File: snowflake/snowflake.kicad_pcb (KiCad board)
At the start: 2 copper layers, 150.2 x 150.2 mm, 85 parts, among them J3 TC2030, SW1 SK-12E12-G040, U1 TZ-5050S2RGB-5V-I4-H1, U10 TZ-5050S2RGB-5V-I4-H1, U11 TZ-5050S2RGB-5V-I4-H1, U12 TZ-5050S2RGB-5V-I4-H1, U13 TZ-5050S2RGB-5V-I4-H1, U14 TZ-5050S2RGB-5V-I4-H1, U15 TZ-5050S2RGB-5V-I4-H1, U16 TZ-5050S2RGB-5V-I4-H1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

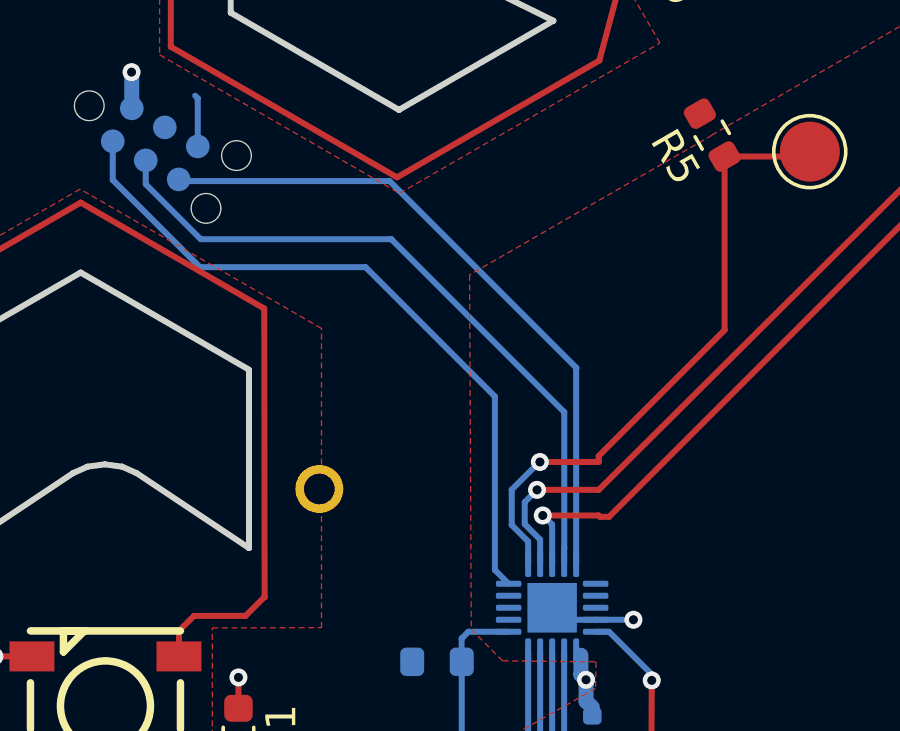
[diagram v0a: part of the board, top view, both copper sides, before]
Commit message: Add more vias to try and keep the ground planes even
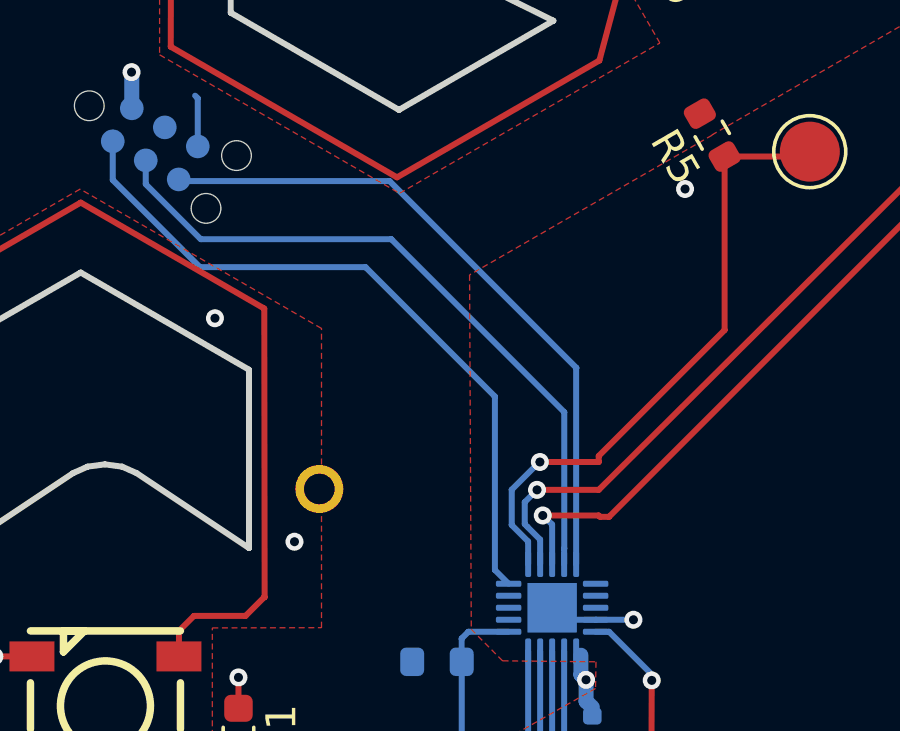
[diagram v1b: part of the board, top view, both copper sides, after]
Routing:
- net GND: vias 50 -> 53
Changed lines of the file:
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@@
+	)
+	(via
+		(at 135.090399 132.750272)
+		(size 0.6)
+		(drill 0.3)
+		(layers "F.Cu" "B.Cu")
+		(free yes)
+		(net 2)
 	)
 	(via
@@
 		(net 2)
 	)
+	(via
+		(at 122.071621 144.507554)
+		(size 0.6)
+		(drill 0.3)
+		(layers "F.Cu" "B.Cu")
+		(free yes)
+		(net 2)
+	)
+	(via
+		(at 119.420449 137.058398)
+		(size 0.6)
+		(drill 0.3)
+		(layers "F.Cu" "B.Cu")
+		(free yes)
+		(net 2)
+	)

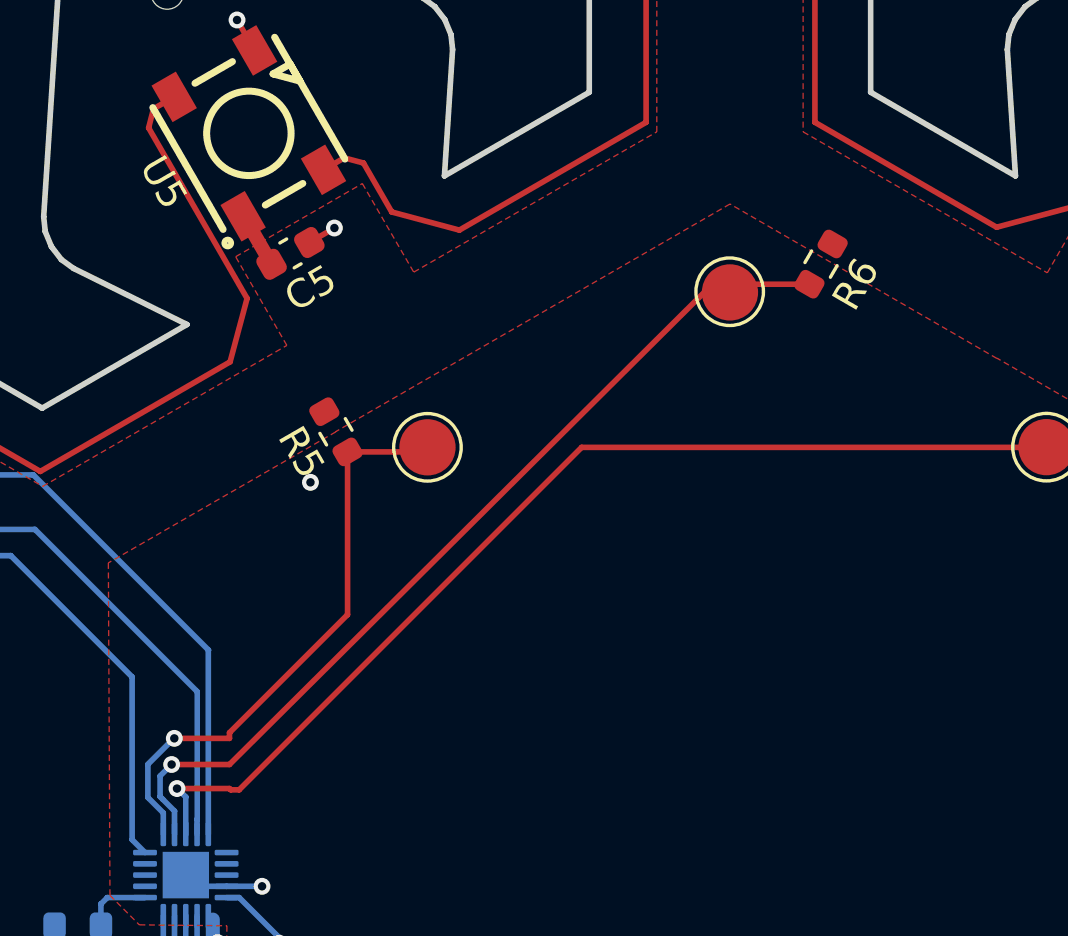
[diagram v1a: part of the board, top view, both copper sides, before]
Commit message: Add teardrops to vias and PTH pads, mask border
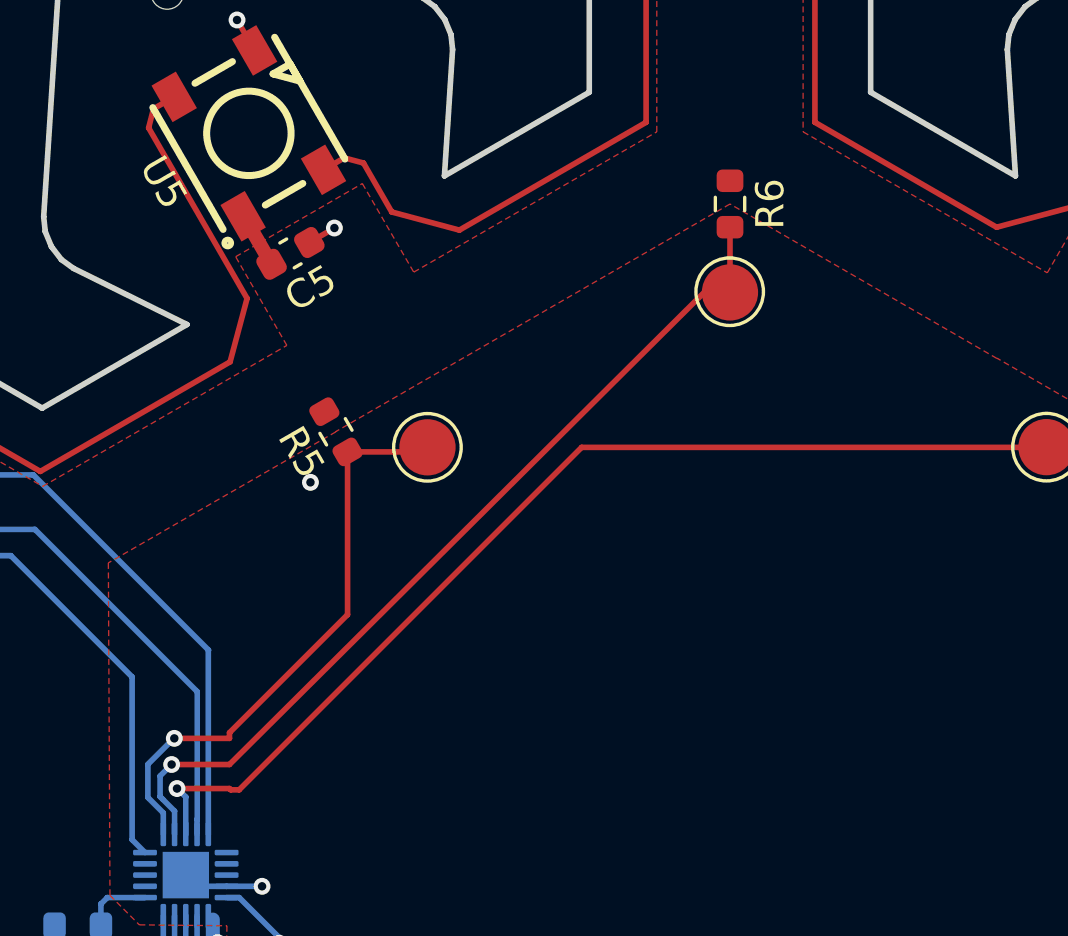
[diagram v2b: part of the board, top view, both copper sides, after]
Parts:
- moved R6 3.88 mm to (150.0, 122.9), turned to -90 degrees
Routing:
- net /TOUCH2: track 32.6 -> 32.0 mm

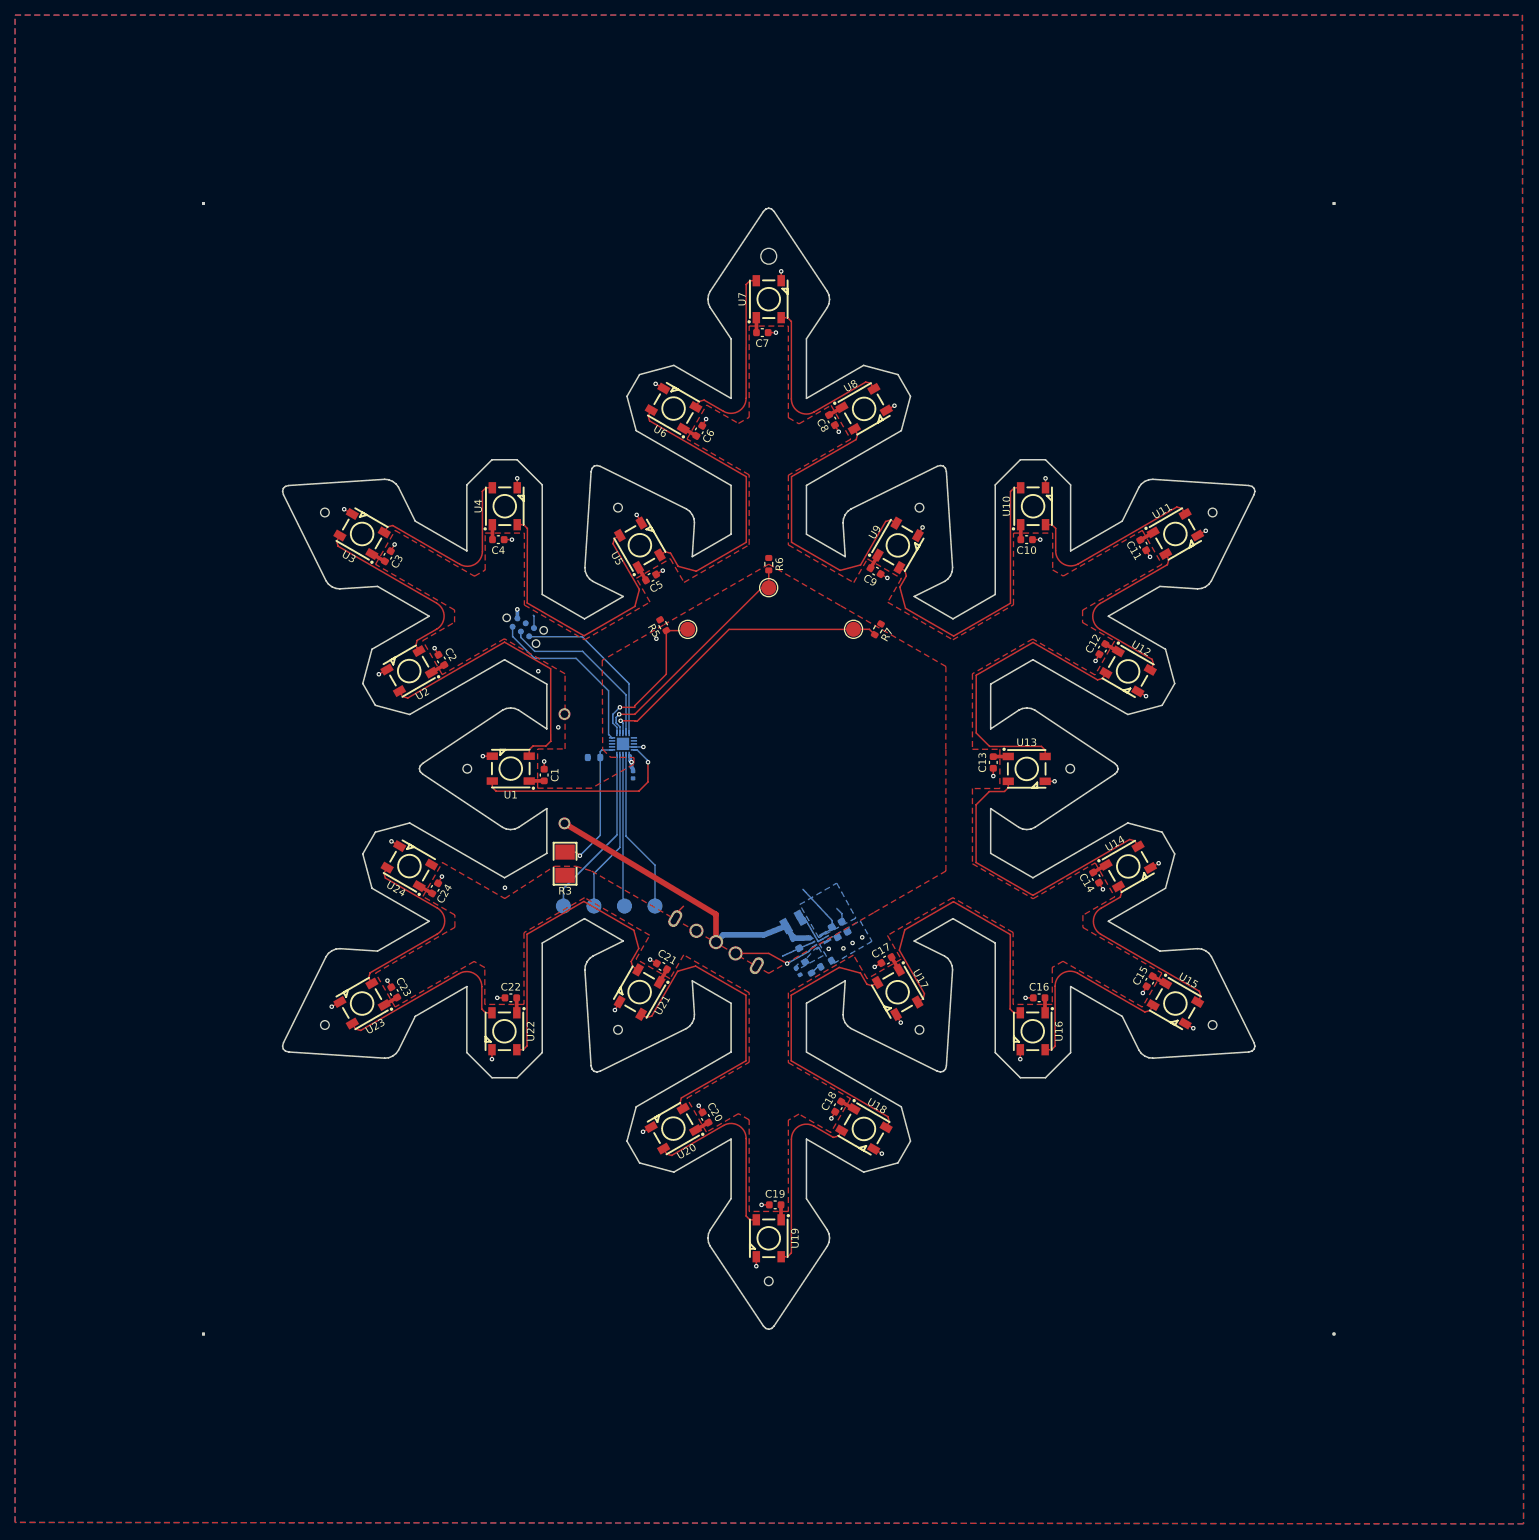
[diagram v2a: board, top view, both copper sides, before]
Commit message: put everything on one side
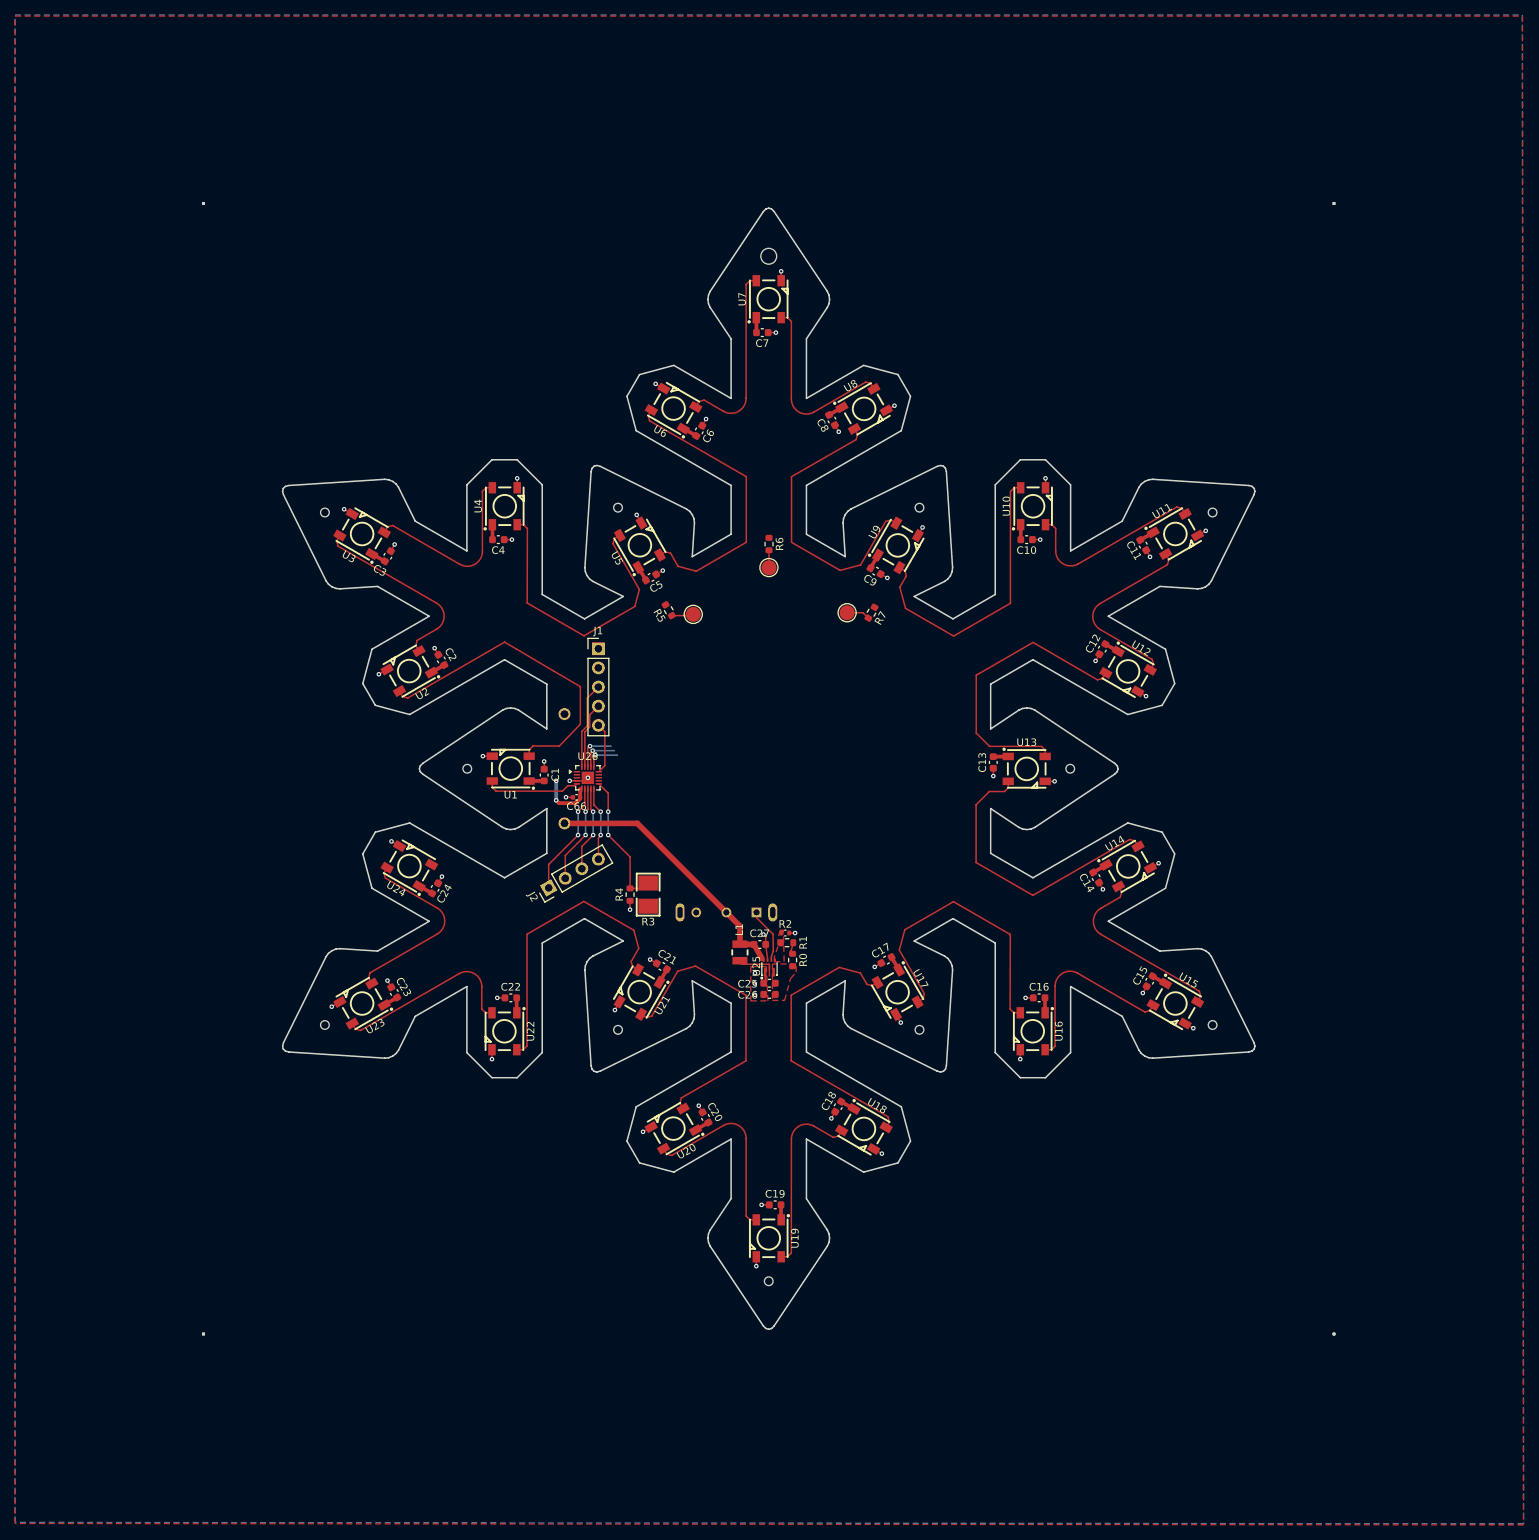
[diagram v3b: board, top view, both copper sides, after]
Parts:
- removed J3: TC2030, Connector:Tag-Connect_TC2030-IDC-NL_2x03_P1.27mm_Vertical
- removed SW1: SK-12E12-G040, easyeda2kicad:SW-TH_SK-12E12-G040
- removed TP1: PC3, TestPoint:TestPoint_Pad_D2.0mm
- removed TP2: PC2, TestPoint:TestPoint_Pad_D2.0mm
- removed TP3: PC1, TestPoint:TestPoint_Pad_D2.0mm
- removed TP4: PC0, TestPoint:TestPoint_Pad_D2.0mm
- added J1: Conn_01x05_Pin, Connector_PinHeader_2.54mm:PinHeader_1x05_P2.54mm_Vertical, F.Cu at (127.4, 134.1)
- added J2: Conn_01x04_Pin, Connector_PinHeader_2.54mm:PinHeader_1x04_P2.54mm_Vertical, F.Cu at (120.8, 165.8)
- added S1: SLW-1277545-3A-RA-N-D, Digikey:SW_SLW-1277545-3A-RA-N-D, B.Cu at (144.4, 169.1)
- C25, C26, C27, C66, L1, R0, R1, R2, R4, U25, U26: moved to F.Cu
- moved R4 18.8 mm to (131.6, 166.7), turned to -90 degrees
- moved C26 13.4 mm to (150.1, 179.9), turned to 180 degrees
- moved R3 11.8 mm to (134.0, 166.7)
- moved C25 11.0 mm to (150.1, 178.5), turned to 180 degrees
- moved L1 8.15 mm to (146.2, 174.4), turned to 90 degrees
- moved C66 8.08 mm to (124.5, 153.8), turned to 180 degrees
- moved U25 7.51 mm to (150.1, 176.2), turned to 90 degrees
- moved U26 6.47 mm to (126.0, 151.2), turned to 0 degrees
- moved R2 5.37 mm to (152.2, 171.8), turned to 0 degrees
- moved C27 4.84 mm to (148.8, 173.3), turned to 180 degrees
- moved R0 4.48 mm to (153.2, 175.4), turned to -90 degrees
- moved R1 4.35 mm to (152.4, 173.1), turned to 180 degrees
- moved TP6 2.67 mm to (150.0, 123.3)
- moved R6 2.67 mm to (150.0, 120.2)
- moved R7 2.36 mm to (163.6, 129.3)
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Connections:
- U26 pad 16: /TOUCH1 -> /TOUCH3
- U26 pad 18: /TOUCH3 -> /TOUCH1
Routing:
- net /TOUCH3: track 40.8 -> 7.33 mm
- net /TOUCH2: track 32.0 -> 8.28 mm
- net /SWIO: track 23.4 -> 6.84 mm
- net /DIN: track 27.5 -> 12.7 mm, vias 1 -> 0
- net /RX: track 23.0 -> 8.80 mm
- net Net-(J2-Pin_4): track 23.0 -> 9.85 mm, vias 0 -> 2
- net /TOUCH1: track 20.8 -> 8.64 mm
- net GND: track 76.5 -> 65.4 mm, vias 53 -> 57
- net /TX: track 22.4 -> 11.5 mm
- net Net-(J2-Pin_3): track 21.5 -> 11.4 mm, vias 0 -> 2
- net Net-(J2-Pin_2): track 20.1 -> 13.1 mm, vias 0 -> 2
- net Net-(J2-Pin_1): track 21.7 -> 15.1 mm, vias 0 -> 2
- net /BAT+: track 41.1 -> 35.4 mm
- net Net-(U1-DOU): track 37.2 -> 42.1 mm
- net /EN: track 11.5 -> 7.10 mm, vias 1 -> 0
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- added copper zone on F.Cu, net Net-(U25-FB)
- removed copper zone on B.Cu, net +5V
- removed copper zone on B.Cu, net Net-(U25-FB)
